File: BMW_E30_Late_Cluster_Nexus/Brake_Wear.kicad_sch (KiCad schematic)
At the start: 12 parts, among them Q1 BC327

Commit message: All Footprints Added to Nexus
All footprints have been added to the nexus board project. Next step is to import them to the layout.
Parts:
- D7, D8: footprint Diode_THT:D_DO-41_SOD81_P10.16mm_Horizontal -> Diode_THT:D_DO-41_SOD81_P12.70mm_Horizontal
- LA10: footprint mount:B8.5d -> BMW_Cluster_Connectors:2721MF
- Q1: footprint Package_TO_SOT_THT:TO-92_Inline -> Package_TO_SOT_THT:TO-92_Inline_Wide
- R100, R101, R11, R9: footprint (none) -> Resistor_THT:R_Axial_DIN0207_L6.3mm_D2.5mm_P15.24mm_Horizontal
- R12: footprint (none) -> Resistor_THT:R_Axial_DIN0309_L9.0mm_D3.2mm_P15.24mm_Horizontal
- R5: footprint (none) -> Resistor_THT:R_Axial_DIN0414_L11.9mm_D4.5mm_P20.32mm_Horizontal
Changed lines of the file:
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@@
 			)
 		)
-		(property "Footprint" "Diode_THT:D_DO-41_SOD81_P10.16mm_Horizontal"
+		(property "Footprint" "Diode_THT:D_DO-41_SOD81_P12.70mm_Horizontal"
 			(at 156.845 67.31 0)
 			(effects
@@
 		(exclude_from_sim no)
 		(in_bom yes)
-		(on_board yes)
+		(on_board no)
 		(dnp yes)
 		(fields_autoplaced yes)
@@
 			)
 		)
-		(property "Footprint" "Package_TO_SOT_THT:TO-92_Inline"
+		(property "Footprint" "Package_TO_SOT_THT:TO-92_Inline_Wide"
 			(at 154.94 81.915 0)
 			(effects
@@
 			)
 		)
-		(property "Footprint" ""
+		(property "Footprint" "Resistor_THT:R_Axial_DIN0309_L9.0mm_D3.2mm_P15.24mm_Horizontal"
 			(at 132.08 85.598 90)
 			(effects
@@
 			)
 		)
-		(property "Footprint" ""
+		(property "Footprint" "Resistor_THT:R_Axial_DIN0207_L6.3mm_D2.5mm_P15.24mm_Horizontal"
 			(at 226.822 102.87 90)
 			(effects
@@
 			)
 		)
-		(property "Footprint" ""
+		(property "Footprint" "Resistor_THT:R_Axial_DIN0414_L11.9mm_D4.5mm_P20.32mm_Horizontal"
 			(at 92.71 110.998 90)
 			(effects
@@
 			)
 		)
-		(property "Footprint" ""
+		(property "Footprint" "Resistor_THT:R_Axial_DIN0207_L6.3mm_D2.5mm_P15.24mm_Horizontal"
 			(at 116.078 76.2 90)
 			(effects
@@
 			)
 		)
-		(property "Footprint" "Diode_THT:D_DO-41_SOD81_P10.16mm_Horizontal"
+		(property "Footprint" "Diode_THT:D_DO-41_SOD81_P12.70mm_Horizontal"
 			(at 198.755 85.09 0)
 			(effects
@@
 			)
 		)
-		(property "Footprint" ""
+		(property "Footprint" "Resistor_THT:R_Axial_DIN0207_L6.3mm_D2.5mm_P15.24mm_Horizontal"
 			(at 122.428 93.98 90)
 			(effects
@@
 		(exclude_from_sim no)
 		(in_bom yes)
-		(on_board yes)
+		(on_board no)
 		(dnp yes)
 		(fields_autoplaced yes)
@@
 			)
 		)
-		(property "Footprint" "mount:B8.5d"
+		(property "Footprint" "BMW_Cluster_Connectors:2721MF"
 			(at 228.6 118.11 90)
 			(effects
@@
 			)
 		)
-		(property "Footprint" ""
+		(property "Footprint" "Resistor_THT:R_Axial_DIN0207_L6.3mm_D2.5mm_P15.24mm_Horizontal"
 			(at 217.678 85.09 90)
 			(effects

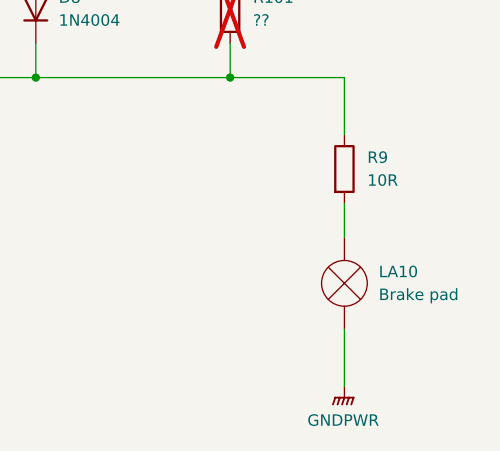
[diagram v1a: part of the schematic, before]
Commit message: Nexus Layout Updates
Layout is about 50% complete. Need to verify exact component locations with early model board.
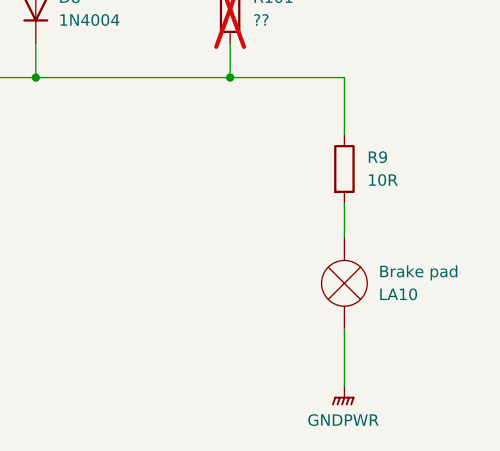
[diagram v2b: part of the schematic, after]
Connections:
- net GNDPWR: now also LA10.1 (-); no longer LA10.2 (+)
- net at R9.2: now also LA10.2 (+); no longer LA10.1 (-)
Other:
- moved on the sheet: LA10
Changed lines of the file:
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@@
+	(wire
+		(pts
+			(xy 228.6 99.06) (xy 228.6 92.71)
+		)
+		(stroke
+			(width 0)
+			(type default)
+		)
+	)
+	(wire
+		(pts
+			(xy 120.65 97.79) (xy 120.65 104.14)
+		)
+		(stroke
+			(width 0)
+			(type default)
+		)
+	)
+	(wire
+		(pts
+			(xy 114.3 68.58) (xy 114.3 72.39)
+		)
+		(stroke
+			(width 0)
+			(type default)
+		)
+	)
+	(wire
+		(pts
+			(xy 172.72 92.71) (xy 194.31 92.71)
+		)
+		(stroke
+			(width 0)
+			(type default)
+		)
+	)
+	(wire
+		(pts
+			(xy 215.9 92.71) (xy 194.31 92.71)
+		)
+		(stroke
+			(width 0)
+			(type default)
+		)
+	)
+	(wire
+		(pts
+			(xy 96.52 68.58) (xy 96.52 72.39)
+		)
+		(stroke
+			(width 0)
+			(type default)
+		)
+	)
 	(wire
 		(pts
 			(xy 228.6 120.65) (xy 228.6 127)
-		)
-		(stroke
-			(width 0)
-			(type default)
-		)
-	)
-	(wire
-		(pts
-			(xy 228.6 99.06) (xy 228.6 92.71)
-		)
-		(stroke
-			(width 0)
-			(type default)
-		)
-	)
-	(wire
-		(pts
-			(xy 120.65 97.79) (xy 120.65 104.14)
-		)
-		(stroke
-			(width 0)
-			(type default)
-		)
-	)
-	(wire
-		(pts
-			(xy 114.3 68.58) (xy 114.3 72.39)
-		)
-		(stroke
-			(width 0)
-			(type default)
-		)
-	)
-	(wire
-		(pts
-			(xy 172.72 92.71) (xy 194.31 92.71)
-		)
-		(stroke
-			(width 0)
-			(type default)
-		)
-	)
-	(wire
-		(pts
-			(xy 215.9 92.71) (xy 194.31 92.71)
-		)
-		(stroke
-			(width 0)
-			(type default)
-		)
-	)
-	(wire
-		(pts
-			(xy 96.52 68.58) (xy 96.52 72.39)
 		)
 		(stroke
@@
 	(symbol
 		(lib_id "Device:Lamp")
-		(at 228.6 115.57 180)
-		(unit 1)
-		(exclude_from_sim no)
-		(in_bom yes)
-		(on_board yes)
-		(dnp no)
-		(fields_autoplaced yes)
+		(at 228.6 115.57 0)
+		(mirror y)
+		(unit 1)
+		(exclude_from_sim no)
+		(in_bom yes)
+		(on_board yes)
+		(dnp no)
 		(property "Reference" "LA10"
-			(at 232.41 114.2999 0)
+			(at 232.41 116.8401 0)
 			(effects
 				(font
@@
 		)
 		(property "Value" "Brake pad"
-			(at 232.41 116.8399 0)
+			(at 232.41 114.3001 0)
 			(effects
 				(font
@@
 		)
 		(property "Footprint" "BMW_Cluster_Connectors:2721MF"
-			(at 228.6 118.11 90)
+			(at 228.6 113.03 90)
 			(effects
 				(font
@@
 		)
 		(property "Datasheet" "~"
-			(at 228.6 118.11 90)
-			(effects
-				(font
+			(at 228.6 113.03 90)
+			(effects
+				(font

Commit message: Added Project Files + Updates
Added project files for SI LED daughter board and speedometer board. Started on reverse engineering schematic for late model SI board.

Also updated some formatting on the nexus board schematic.
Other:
- company: (none) -> Reagan Ansel
- moved on the sheet: C1, C2, D7, D8, LA10, Q1, R100, R101, R11, R12, R5, R9

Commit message: Update Schematic PDFs
Added updates to schematic pdf documents for consistency
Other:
- company: Reagan Ansel -> Reans
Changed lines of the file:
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@@
 		(date "2025-11-10")
 		(rev "0")
-		(company "Reagan Ansel")
+		(company "Reans")
+		(comment 1 "Reagan Ansel")
 	)
 	(junction
